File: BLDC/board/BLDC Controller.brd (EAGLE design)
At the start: 100 x 70.3 mm, 113 parts, among them IC1 DRV8301, IC2 OPA2374, IC3 Encoder, IC4 INA199A1, IC5 TPS51103, M1 FRDM-KL05Z, M2 MBED_NXP_LPC1768, Q1 MOSFET-NCHANNELSMD, Q2 MOSFET-NCHANNELSMD, Q3 P-CHANNEL-MOSFETTO252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

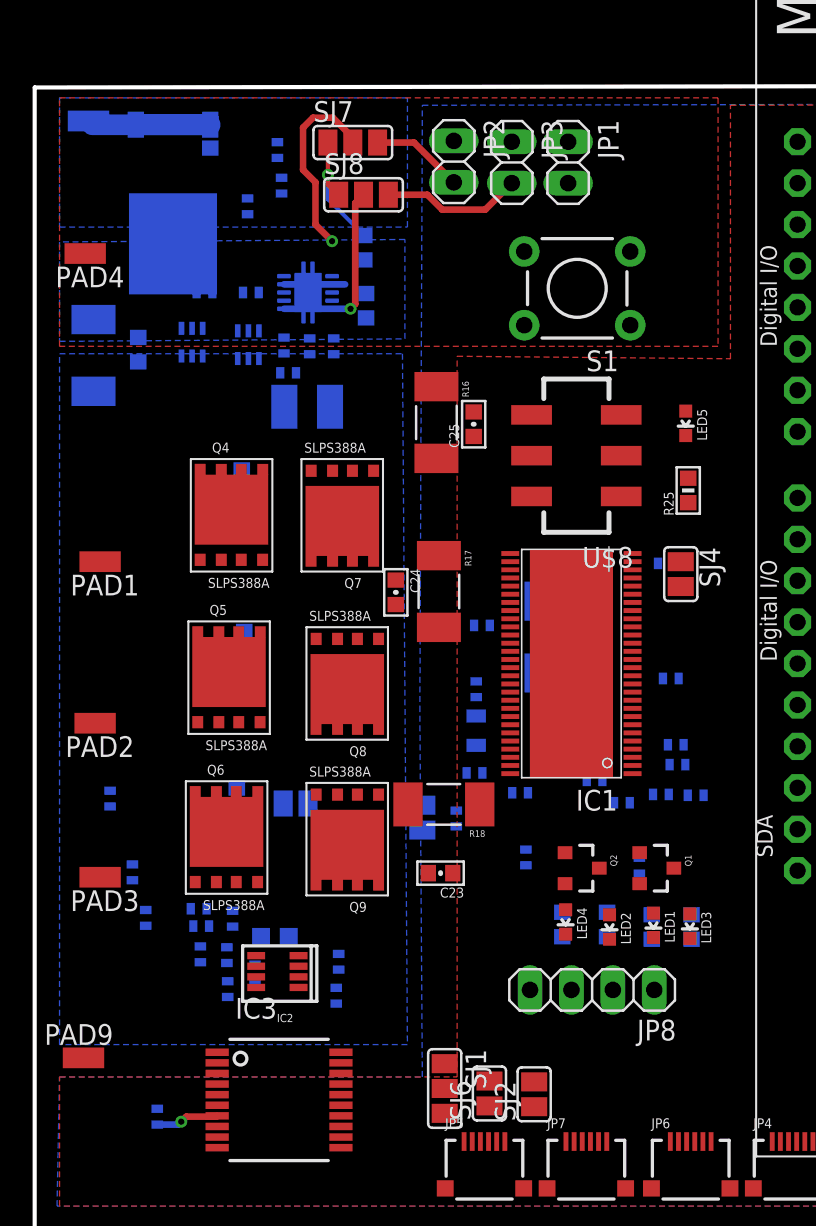
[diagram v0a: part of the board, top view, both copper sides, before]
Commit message: Routed power management (Reverse Polarity, battery sense, vreg) section.
245 airwires.
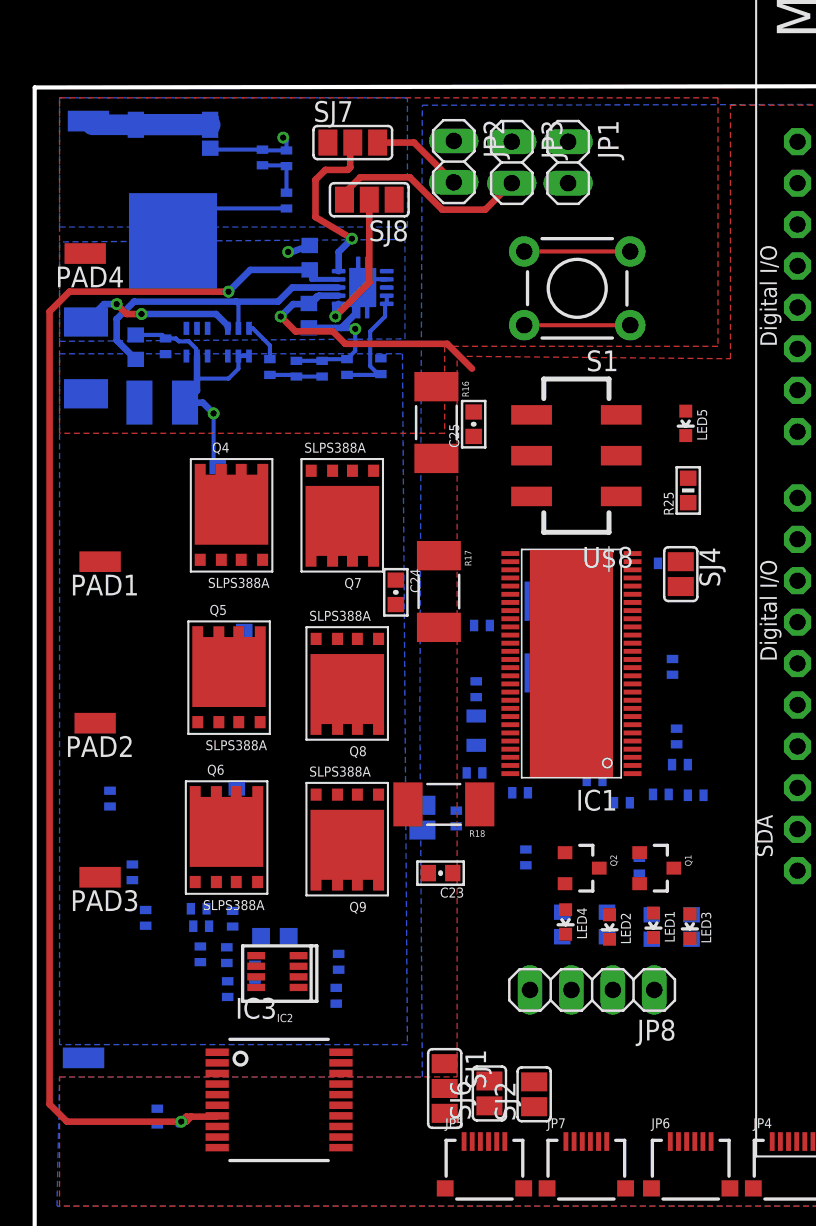
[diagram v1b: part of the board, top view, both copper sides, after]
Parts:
- moved R27 9.86 mm to (19.2, 52.8), turned to 90 degrees
- moved R28 9.17 mm to (21.2, 52.9), turned to 270 degrees
- moved C18 8.89 mm to (7.82, 50.6), turned to 180 degrees
- moved C19 7.69 mm to (8.03, 54.1), turned to 90 degrees
- moved C31 5.38 mm to (16.8, 56.0), turned to 270 degrees
- moved C32 4.54 mm to (16.9, 59.5), turned to 90 degrees
- moved SJ5 3.56 mm to (18.6, 23.6), turned to 270 degrees
- moved IC5 3.37 mm to (20.1, 56.4)
- moved R26 2.41 mm to (15.4, 63.0), turned to 270 degrees
- moved R29 1.70 mm to (15.4, 65.6)
- moved R39 1.59 mm to (16.1, 52.7), turned to 270 degrees
- moved R38 1.58 mm to (14.4, 52.8), turned to 90 degrees
- moved C37 1.55 mm to (17.6, 52.7), turned to 90 degrees
- moved C17 1.49 mm to (11.2, 46.0), turned to 90 degrees
- moved C29 1.02 mm to (14.0, 65.7)
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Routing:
- net 5V: track 7.65 -> 79.8 mm, vias 1 -> 2
- net GND: track 9.08 -> 37.1 mm, vias 1 -> 4
- net 3.3V: track 0.00 -> 19.2 mm, vias 0 -> 1
- net V_BATT: track 0.00 -> 19.1 mm
- net I_BATT: track 0.00 -> 17.7 mm, vias 0 -> 2
- net PWR_ENABLE1: track 0.00 -> 7.71 mm
- net RST_05Z: track 0.00 -> 6.50 mm
- net 05Z_3.3V: track 0.00 -> 6.50 mm
- net N$13: track 8.62 -> 12.6 mm
- net SENSE_I_BATT: track 0.00 -> 3.31 mm
- net SENSE_V_BATT: track 0.00 -> 3.15 mm
- net N$18: track 0.00 -> 2.55 mm
- net V3IN1: track 11.4 -> 8.89 mm

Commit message: Added 3 planes for SH_A,SH_B, SH_C. Modifired DRV thermal footprint to be consistant with datasheet. Routed a lot of the DRV-components through the gap added by the right footprint.
Down to 163 airwires.
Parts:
- moved C23 13.6 mm to (25.3, 35.4), turned to 270 degrees
- moved C24 13.5 mm to (25.3, 25.9)
- moved SJ4 12.5 mm to (38.4, 52.5), turned to 90 degrees
- moved C8 9.87 mm to (27.4, 34.9)
- moved R7 6.20 mm to (40.4, 33.6), turned to 270 degrees
- moved C21 6.11 mm to (6.76, 35.4)
- moved R17 5.58 mm to (22.6, 33.9), turned to 90 degrees
- moved R16 5.46 mm to (22.8, 44.3), turned to 90 degrees
- moved C17 5.26 mm to (6.05, 46.9)
- moved C5 5.19 mm to (39.3, 38.5), turned to 90 degrees
- moved C25 4.98 mm to (25.5, 44.6), turned to 270 degrees
- moved C4 4.36 mm to (38.5, 35.4)
- moved C22 3.97 mm to (8.43, 26.1)
- moved R18 3.03 mm to (22.5, 24.4), turned to 90 degrees
- moved Q4 2.29 mm to (12.0, 46.9)
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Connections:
- net GND: now also IC1.EXP@1
- net SS_TR: no longer IC1.EXP@1
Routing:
- net V_BATT: track 19.1 -> 45.6 mm, vias 0 -> 15
- net 3.3V: track 19.2 -> 40.4 mm, vias 1 -> 4
- net DRV_MISO: track 0.00 -> 15.4 mm
- net DRV_MOSI: track 0.00 -> 15.4 mm
- net CS_DRV: track 0.00 -> 15.0 mm
- net EN_GATE: track 0.00 -> 14.2 mm
- net SL_A: track 0.00 -> 10.0 mm
- net SL_C: track 0.00 -> 9.07 mm
- net SL_B: track 0.00 -> 9.03 mm
- net PH: track 0.00 -> 7.66 mm, vias 0 -> 1
- net CP1: track 0.00 -> 5.01 mm, vias 0 -> 1
- net CP2: track 0.00 -> 4.82 mm, vias 0 -> 1
- net BST_C: track 0.00 -> 4.49 mm, vias 0 -> 1
- net SH_C: track 0.00 -> 4.44 mm, vias 0 -> 1
- net BST_B: track 0.00 -> 4.44 mm, vias 0 -> 1
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- added copper zone on layer 1, net SH_A
- added copper zone on layer 1, net SH_B
- added copper zone on layer 1, net SH_C

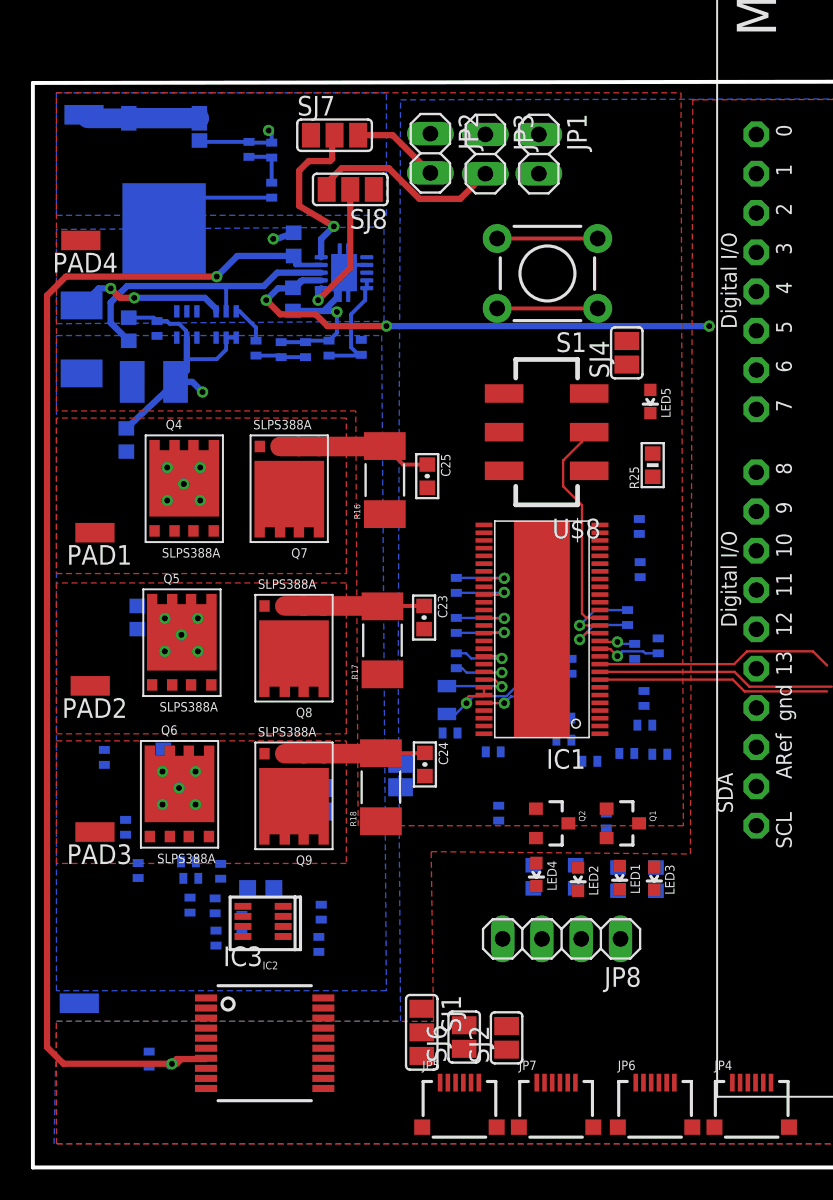
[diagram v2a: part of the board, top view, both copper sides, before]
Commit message: 97 airwires.
Most of the powermosfets are routed.
Most of the encoder is routed
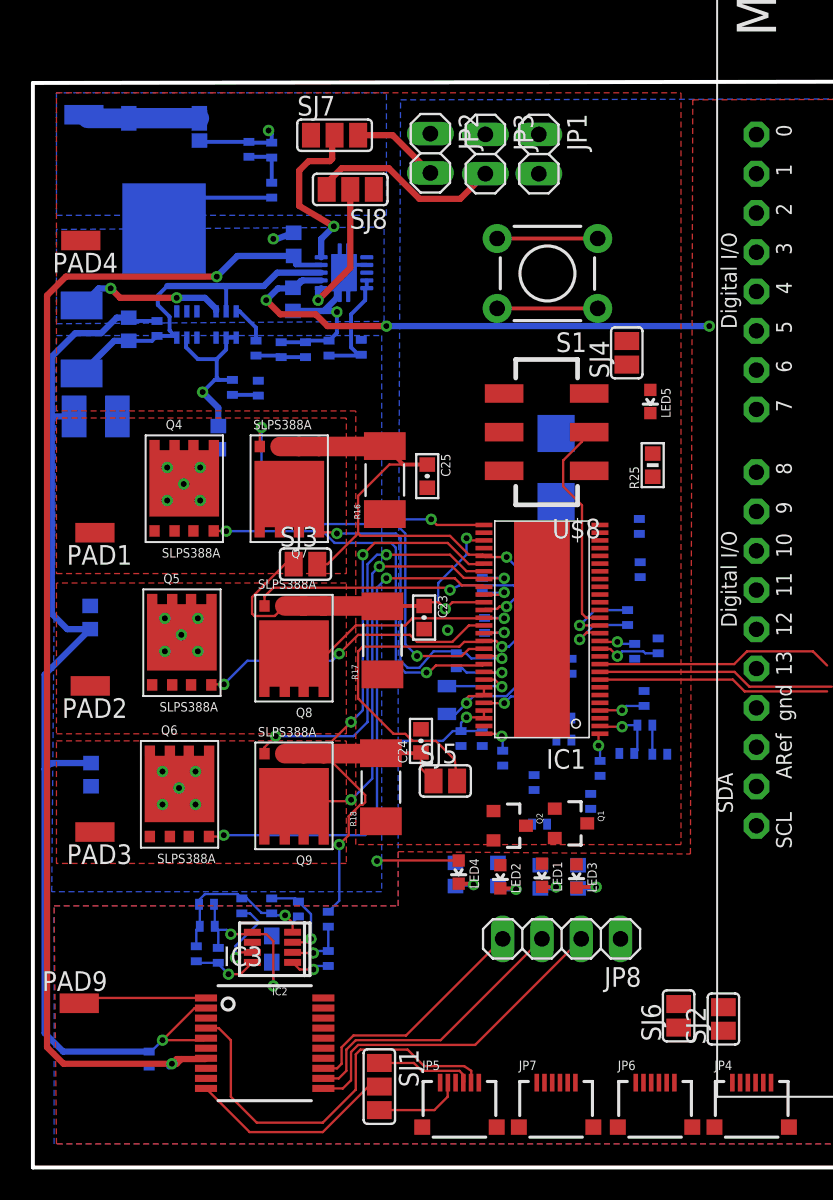
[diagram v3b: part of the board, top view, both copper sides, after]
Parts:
- moved R12 29.7 mm to (14.6, 50.2), turned to 90 degrees
- moved C20 25.3 mm to (12.9, 50.3), turned to 90 degrees
- moved C15 23.8 mm to (29.1, 27.6)
- moved SJ3 15.0 mm to (17.6, 38.9), flipped to the top, turned to 0 degrees
- moved SJ2 14.1 mm to (44.7, 9.45)
- moved SJ6 13.9 mm to (41.8, 9.65)
- moved D1 9.25 mm to (33.8, 45.1)
- moved SJ5 8.17 mm to (26.7, 24.8), flipped to the top, turned to 0 degrees
- moved R24 6.09 mm to (15.4, 16.8), turned to 270 degrees
- moved C14 5.99 mm to (36.1, 23.5)
- moved C17 5.95 mm to (12.0, 47.0)
- moved R21 5.59 mm to (17.2, 16.6)
- moved LED1 5.03 mm to (32.9, 18.7)
- moved LED2 5.03 mm to (30.2, 18.6)
- moved LED3 5.03 mm to (35.2, 18.7)
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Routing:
- net GND: track 38.1 -> 116.4 mm, vias 4 -> 7
- net SL_A: track 10.0 -> 60.8 mm, vias 0 -> 2
- net SL_C: track 9.07 -> 46.1 mm, vias 0 -> 3
- net GH_C: track 0.00 -> 33.9 mm, vias 0 -> 2
- net GL_A: track 0.00 -> 29.7 mm, vias 0 -> 2
- net V_BATT: track 45.6 -> 72.6 mm, vias 15 -> 18
- net ENC_CS: track 0.00 -> 26.4 mm
- net GL_C: track 0.00 -> 26.2 mm, vias 0 -> 2
- net GH_A: track 0.00 -> 25.9 mm, vias 0 -> 2
- net SH_C: track 4.44 -> 29.4 mm, vias 1 -> 3
- net U: track 0.00 -> 21.8 mm
- net GL_B: track 0.00 -> 20.5 mm, vias 0 -> 2
- net GH_B: track 0.00 -> 19.6 mm, vias 0 -> 2
- net V: track 0.00 -> 18.7 mm
- net SL_B: track 9.03 -> 27.2 mm, vias 0 -> 2
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
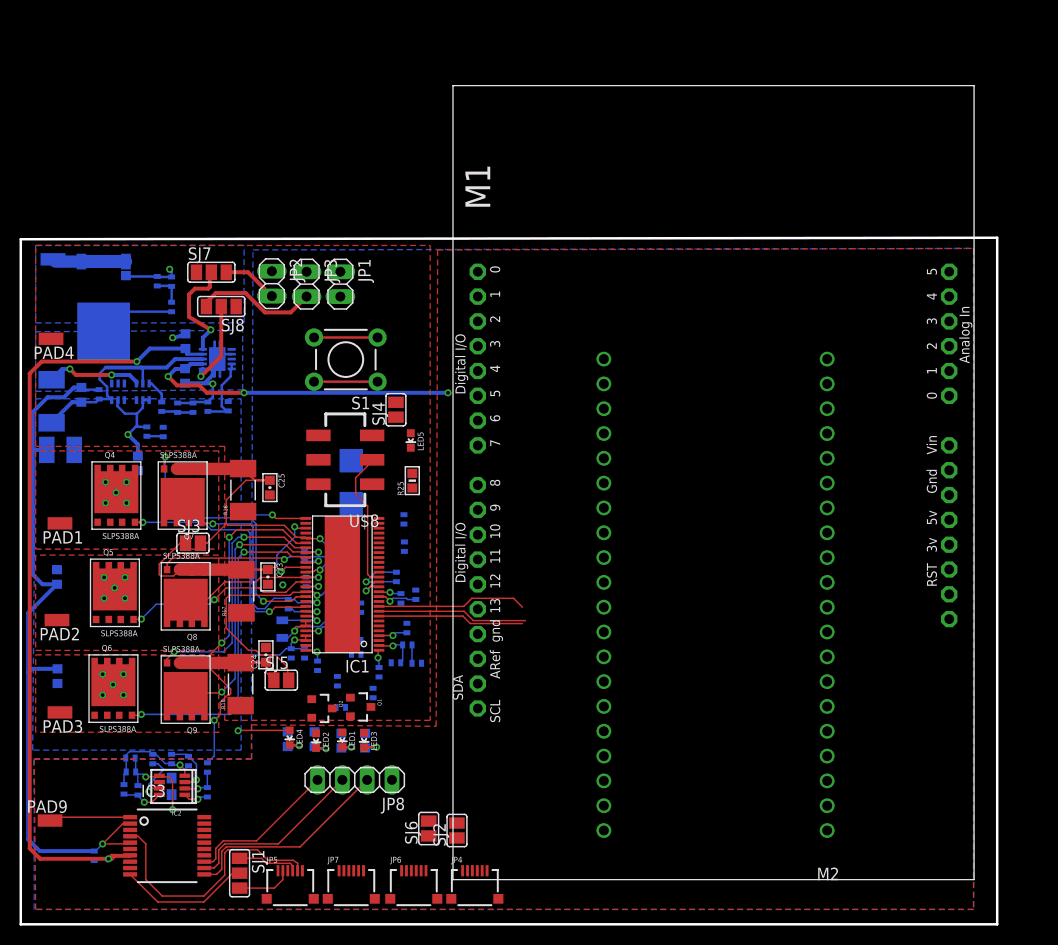
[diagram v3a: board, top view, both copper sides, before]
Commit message: 11 airwires left.
Made major routes everywhere.  Need to think, clear head, and clean up some of the connections.

Some connections are getting 3+ vias, which can be improved w/ thought.
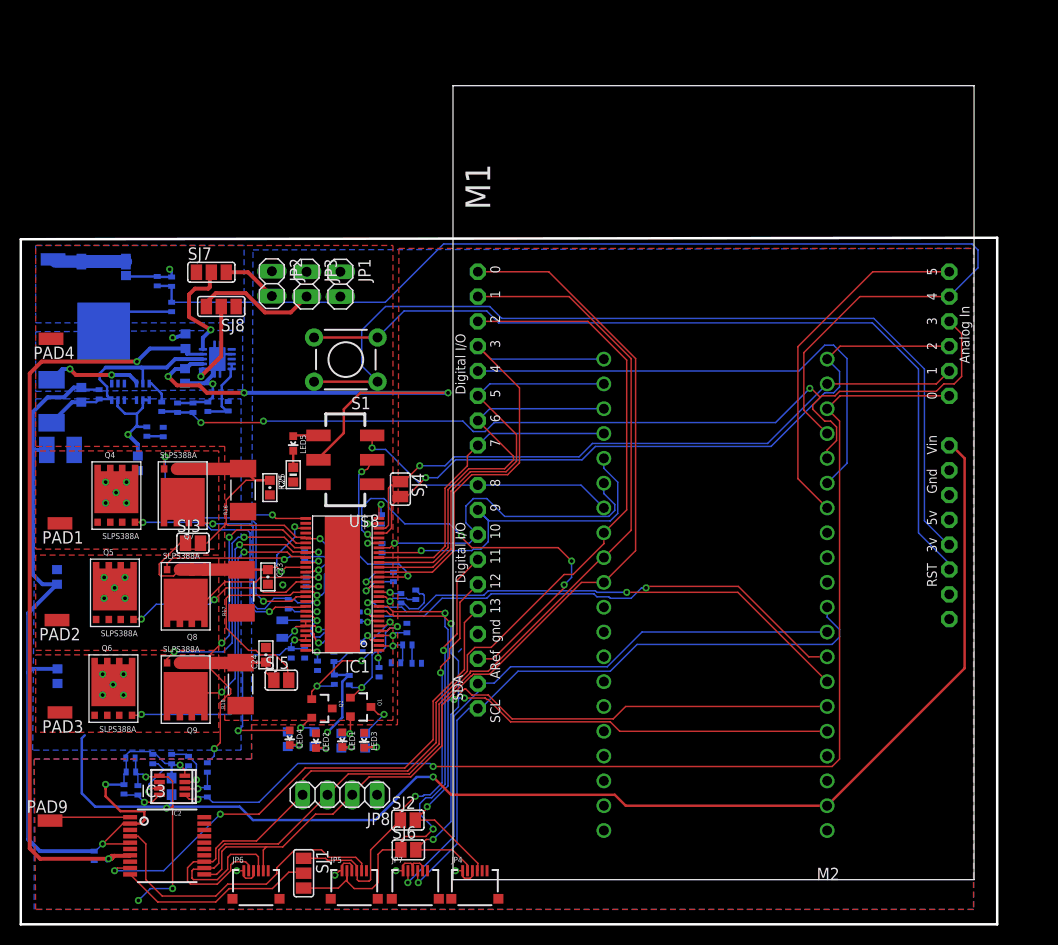
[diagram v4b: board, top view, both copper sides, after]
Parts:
- moved JP6 16.2 mm to (24.1, 3.61)
- moved R25 12.2 mm to (27.9, 45.9)
- moved LED5 12.0 mm to (27.9, 49.1)
- moved D1 8.42 mm to (33.1, 36.7)
- moved SJ4 8.14 mm to (38.9, 44.4), turned to 270 degrees
- moved JP7 6.55 mm to (40.4, 3.61)
- moved JP5 6.55 mm to (34.1, 3.61)
- moved SJ1 6.55 mm to (29.0, 5.08)
- moved C14 5.46 mm to (32.1, 27.2), turned to 270 degrees
- moved SJ2 5.14 mm to (39.6, 10.5), turned to 0 degrees
- moved SJ6 3.02 mm to (39.7, 7.47), turned to 0 degrees
- moved R8 2.92 mm to (33.6, 24.8), turned to 90 degrees
- moved C5 2.29 mm to (37.0, 38.4)
- moved C6 2.29 mm to (36.9, 41.3)
- moved JP8 2.16 mm to (32.7, 13.1)
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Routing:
- net V_BATT: track 72.6 -> 209.8 mm, vias 18 -> 19
- net SENSE_V_BATT: track 3.15 -> 121.0 mm
- net C_I: track 2.59 -> 119.5 mm, vias 1 -> 2
- net SENSE_I_BATT: track 3.31 -> 100.7 mm, vias 0 -> 3
- net W: track 15.7 -> 107.7 mm
- net V: track 18.7 -> 109.5 mm
- net 05Z_3.3V: track 6.50 -> 92.8 mm
- net U: track 21.8 -> 103.5 mm
- net RST_05Z: track 6.50 -> 87.3 mm
- net A_I: track 0.00 -> 71.1 mm, vias 0 -> 1
- net B_I: track 0.00 -> 67.3 mm, vias 0 -> 1
- net SCL: track 0.00 -> 65.9 mm, vias 0 -> 1
- net DRV_MISO: track 15.4 -> 80.1 mm, vias 0 -> 3
- net DRV_MOSI: track 15.4 -> 79.7 mm, vias 0 -> 3
- net SDA: track 0.00 -> 62.7 mm, vias 0 -> 1
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
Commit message: First route with zero airwires.  Still haven't run DRC.
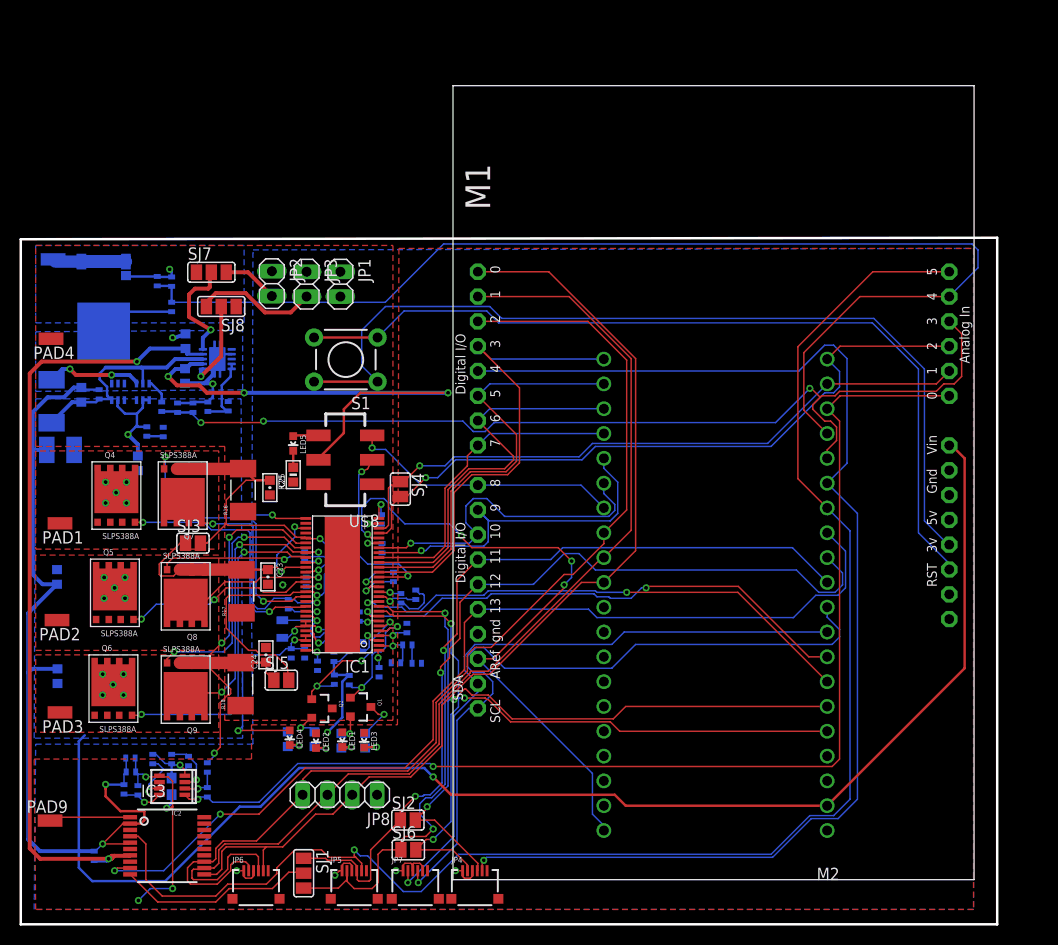
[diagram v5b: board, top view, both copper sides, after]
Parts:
- moved R4 0.07 mm to (35.0, 28.3), turned to 90 degrees
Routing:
- net ENC_CS: track 68.5 -> 156.5 mm, vias 0 -> 1
- net CS_EXT: track 53.1 -> 128.7 mm, vias 0 -> 1
- net ENC_CLK: track 55.1 -> 100.8 mm
- net ENC_MISO: track 44.5 -> 88.5 mm
- net ENC_MOSI: track 51.8 -> 89.5 mm
- net ADC_REF: track 44.2 -> 67.1 mm
- net V_BATT: track 209.8 -> 220.6 mm
- net SCL: track 65.9 -> 74.2 mm
- net SDA: track 62.7 -> 66.4 mm
- net VSENSE: track 3.70 -> 5.31 mm
- net 3.3V: track 102.8 -> 101.3 mm
- net GND: track 155.7 -> 157.1 mm
- net 5V: track 79.8 -> 81.1 mm
- net SL_A: track 59.9 -> 60.6 mm
